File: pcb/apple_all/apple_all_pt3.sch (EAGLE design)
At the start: 47 parts, among them IC1 STM32F072C8T6, SW1 324_SW, SW2 324_SW, SW3 324_SW

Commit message: updated apple_all protocol card
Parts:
- removed U$1: PINHD1X4, adafruit_changed:PINHD1X4
- added JP8: (no value), pinhead:PINHD-1X2
- added R19: 2K, SparkFun-Passives:RESISTOR0805-RES
- R10, R16, R6, R8: value 50 -> 200
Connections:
- removed net N$30: IC1PORTB_L.PB1, JP5.1, R16.1
- new net N$11: IC1PORTB_L.PB1, U$10.4
- net GND: now also JP5.1, R16.1; no longer U$1.1
- net N$3: now also R19.2; no longer U$1.4
- net N$41: no longer U$10.4
- net N$43: no longer U$1.3
- net N$46: now also JP8.1, JP8.2, R19.1; no longer U$1.2

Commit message: added resistors on lisa pins
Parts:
- removed J4: (no value), SparkFun-Connectors:USB_C16PIN
- removed U$10: PINHD1X4, adafruit_changed:PINHD1X4
- added J1: (no value), SparkFun-Connectors:DB9FEMALE
- added R20: 5.1K, SparkFun-Passives:RESISTOR0805-RES
- added R21: 2K, SparkFun-Passives:RESISTOR0805-RES
- added U$1: M2.5HOLE, f1c100s:M2.5HOLE
- J2: device SparkFun-Connectors:DB9FEMALE -> SparkFun-Connectors:USB_C16PIN
- JP1: device adafruit_changed:PINHD-2X20-BIG -> pinhead:PINHD-1X5
- JP2: device pinhead:PINHD-2X3 -> pinhead:PINHD-1X2
- JP3: device pinhead:PINHD-2X4 -> pinhead:PINHD-2X2
- JP4: value AUDIO-JACK4-.25-HORIZ-TRS -> (none); device SparkFun-Connectors:AUDIO-JACK4-.25-HORIZ-TRS -> adafruit_changed:PINHD-2X20-BIG
- JP5: device pinhead:PINHD-2X2 -> pinhead:PINHD-2X3
- JP6: value (none) -> AUDIO-JACK4-.25-HORIZ-TRS; device pinhead:PINHD-1X5 -> SparkFun-Connectors:AUDIO-JACK4-.25-HORIZ-TRS
- JP8: device pinhead:PINHD-1X2 -> pinhead:PINHD-2X4
- R11: value 5.1K -> 200
- R12, R19: value 2K -> 5.1K
- R13, R17: value 5.1K -> 100
- R15: value 2K -> 100
- R16: value 200 -> 5.1K
- R18: value 100 -> 2K
- R6: value 200 -> 2K
- R7: value 2K -> 200
- R9: value 5.1K -> 2K
- U$3: value M2.5HOLE -> PINHD1X4; device f1c100s:M2.5HOLE -> adafruit_changed:PINHD1X4
- U$4: value ADB -> M2.5HOLE; device adb:ADB -> f1c100s:M2.5HOLE
- U$6: value M2.5HOLE -> ADB; device f1c100s:M2.5HOLE -> adb:ADB
- U$8: value PINHD1X4 -> RJ9PTH; device adafruit_changed:PINHD1X4 -> SparkFun-Retired:RJ9PTH
- U$9: value RJ9PTH -> PINHD1X4; device SparkFun-Retired:RJ9PTH -> adafruit_changed:PINHD1X4
- renumbered C7 to C1, C8 to C2, C9 to C3
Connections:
- new net N$30: JP6.RING, R15.1, R16.2
- new net N$32: JP6.TIP, R16.1, R17.1
- net +3V3: now also JP4.1, JP4.17, JP8.5, R12.2, SW3.2, SW3.3; no longer JP1.1, JP1.17, JP3.5, R9.2, SW2.2, SW2.3
- net +5V: now also J2.VBUS, JP4.2, JP4.4; no longer J4.VBUS, JP1.2, JP1.4
- net +7V: now also J1.4; no longer J2.4
- net GND: now also J1.3, J1.5, J1.SHIELD, J2.GND, J2.SHLD, JP3.1, JP4.14, JP4.20, JP4.25, JP4.30, JP4.34, JP4.39, JP4.6, JP4.9, JP5.2, JP8.6, R14.1, R19.2, R20.2, R9.1, SW2.1, SW2.4, U$3.1, U$6.GND, U$6.SHIELD; no longer J2.3, J2.5, J2.SHIELD, J4.GND, J4.SHLD, JP1.14, JP1.20, JP1.25, JP1.30, JP1.34, JP1.39, JP1.6, JP1.9, JP2.1, JP2.2, JP3.6, R14.2, R16.1, R18.2, R7.1, SW3.1, SW3.4, U$4.GND, U$4.SHIELD, U$8.1
- net N$1: now also J2.CC1, R19.1; no longer J4.CC1, R13.1
- net N$10: now also U$8.3; no longer U$9.3
- net N$11: now also U$9.4; no longer U$10.4
- net N$12: now also JP8.7; no longer JP3.7
- net N$13: now also JP4.22, R12.1, SW2.2, SW2.3; no longer JP1.22, R9.1, SW1.2, SW1.3
- net N$14: now also JP8.8; no longer JP3.8
- net N$15: now also JP8.3; no longer JP3.3
- net N$16: now also JP8.4; no longer JP3.4
- net N$17: now also JP3.2, R7.1; no longer JP5.2, R6.1
- net N$18: now also JP4.32, R14.2, SW3.1, SW3.4; no longer JP1.32, R11.2, SW2.1, SW2.4
- net N$19: now also JP3.4; no longer JP5.4
- net N$2: now also R18.2; no longer R12.2
- net N$20: now also U$8.2; no longer U$9.2
- net N$21: now also R11.2, U$8.1; no longer R16.2, U$9.1
- net N$22: now also JP4.5; no longer JP1.5
- net N$23: now also JP4.3; no longer JP1.3
- net N$24: now also JP6.EARTH, R13.1; no longer JP4.EARTH, R18.1
- net N$25: now also JP3.3; no longer JP5.3
- net N$26: now also J1.1, JP1.3; no longer J2.1, JP6.3
- net N$27: now also JP8.1, R21.1; no longer JP3.1, R15.1
- net N$28: now also R21.2; no longer R15.2
- net N$29: now also R9.2; no longer R7.2
- net N$3: now also R6.2, U$3.4, U$6.5V; no longer R19.2, U$4.5V, U$8.4
- net N$31: now also JP5.5, JP5.6, R17.2; no longer JP2.5, JP2.6, JP4.TIP, R17.1
- net N$34: now also J1.6, JP1.2; no longer J2.6, JP6.2
- net N$35: now also J1.7, JP1.5; no longer J2.7, JP6.5
- net N$36: now also J1.2, JP1.1; no longer J2.2, JP6.1
- net N$37: now also JP4.36; no longer JP1.36
- net N$38: now also U$9.1; no longer U$10.1
- net N$39: now also U$9.2; no longer U$10.2
- net N$4: now also J1.8, JP1.4; no longer J2.8, JP6.4
- net N$40: now also U$9.3; no longer U$10.3
- net N$41: now also JP5.3, JP5.4, R15.2; no longer JP2.3, JP2.4, JP4.RING, R17.2
- net N$43: now also U$3.3, U$6.ADB_DATA; no longer U$4.ADB_DATA, U$8.3
- net N$46: now also JP2.1, JP2.2, R6.1, SW1.2, SW1.3, U$3.2, U$6.PSW; no longer JP8.1, JP8.2, R19.1, SW3.2, SW3.3, U$4.PSW, U$8.2
- net N$5: now also R7.2, U$8.4; no longer R6.2, U$9.4
- net N$6: now also JP8.2, R18.1; no longer JP3.2, R12.1
- net N$7: now also J2.CC2, R20.1; no longer J4.CC2, R14.1
- net N$8: now also J2.D+; no longer J4.D+
- net N$9: now also J2.D-; no longer J4.D-
- net SPI_CS: now also JP4.24; no longer JP1.24
- net SPI_MISO: now also JP4.21; no longer JP1.21
- net SPI_MOSI: now also JP4.19; no longer JP1.19
- net SPI_SCK: now also JP4.23; no longer JP1.23
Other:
- moved on the sheet: R11, R12, R13, R14, R15, R16, R17, R18, R19, R6, R7, R9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

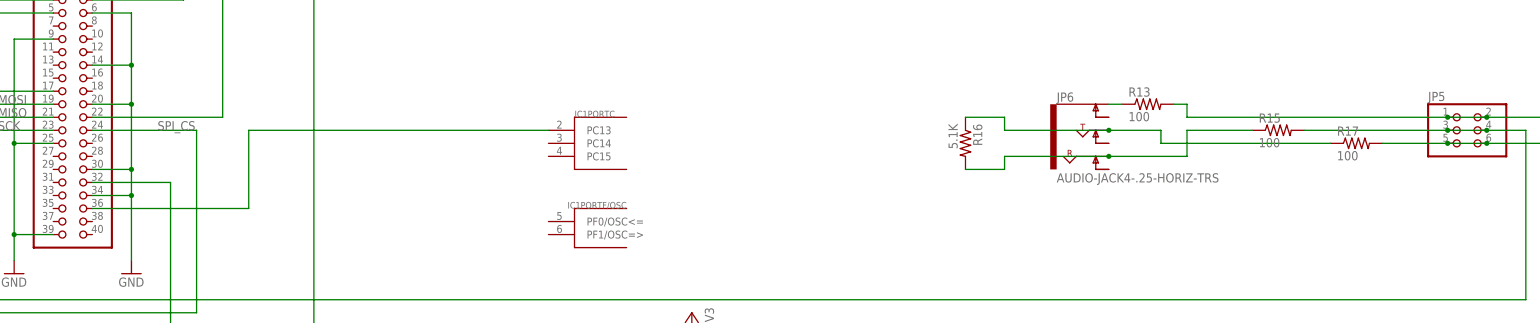
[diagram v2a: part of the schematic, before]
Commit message: added busy pin and adjusted resistors
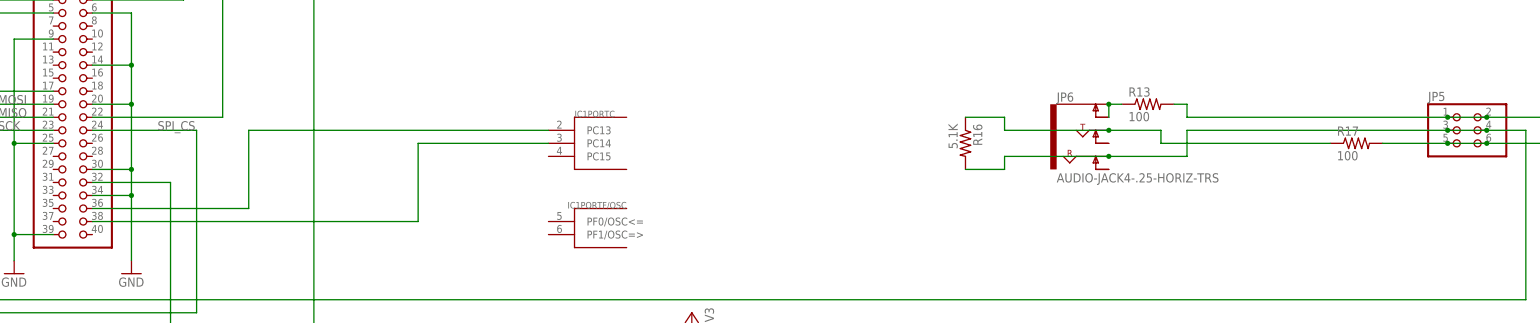
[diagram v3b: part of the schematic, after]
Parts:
- removed R15: 100, SparkFun-Passives:RESISTOR0805-RES
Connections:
- removed net N$41: IC1PORTA_L.PA3, JP5.3, JP5.4, R15.2
- new net N$33: IC1PORTC.PC14, JP4.38
- net N$24: now also JP6.EARTH-NORM
- net N$30: now also IC1PORTA_L.PA3, JP5.3, JP5.4; no longer R15.1
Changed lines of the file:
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@@
 <part name="JP2" library="pinhead" library_urn="urn:adsk.eagle:library:325" deviceset="PINHD-1X2" device="" package3d_urn="urn:adsk.eagle:package:22435/2"/>
 <part name="R6" library="SparkFun-Passives" deviceset="RESISTOR" device="0805-RES" value="2K"/>
-<part name="R15" library="SparkFun-Passives" deviceset="RESISTOR" device="0805-RES" value="100"/>
 <part name="R17" library="SparkFun-Passives" deviceset="RESISTOR" device="0805-RES" value="100"/>
 </parts>
@@
 <attribute name="VALUE" x="-31.242" y="128.27" size="1.778" layer="96" rot="MR90"/>
 </instance>
-<instance part="R15" gate="G$1" x="327.66" y="15.24" smashed="yes">
-<attribute name="NAME" x="323.85" y="16.7386" size="1.778" layer="95"/>
-<attribute name="VALUE" x="323.85" y="11.938" size="1.778" layer="96"/>
-</instance>
 <instance part="R17" gate="G$1" x="342.9" y="12.7" smashed="yes">
 <attribute name="NAME" x="339.09" y="14.1986" size="1.778" layer="95"/>
@@
 <pinref part="U$9" gate="1" pin="3"/>
 <wire x1="43.18" y1="22.86" x2="17.78" y2="22.86" width="0.1524" layer="91"/>
-</segment>
-</net>
-<net name="N$41" class="0">
-<segment>
-<pinref part="IC1" gate="PORTA_L" pin="PA3"/>
-<wire x1="43.18" y1="20.32" x2="20.32" y2="20.32" width="0.1524" layer="91"/>
-<wire x1="20.32" y1="-17.78" x2="375.92" y2="-17.78" width="0.1524" layer="91"/>
-<wire x1="375.92" y1="-17.78" x2="375.92" y2="15.24" width="0.1524" layer="91"/>
-<pinref part="JP5" gate="A" pin="4"/>
-<pinref part="JP5" gate="A" pin="3"/>
-<wire x1="360.68" y1="15.24" x2="368.3" y2="15.24" width="0.1524" layer="91"/>
-<junction x="360.68" y="15.24"/>
-<wire x1="375.92" y1="15.24" x2="368.3" y2="15.24" width="0.1524" layer="91"/>
-<junction x="368.3" y="15.24"/>
-<wire x1="20.32" y1="20.32" x2="20.32" y2="-17.78" width="0.1524" layer="91"/>
-<wire x1="332.74" y1="15.24" x2="360.68" y2="15.24" width="0.1524" layer="91"/>
-<pinref part="R15" gate="G$1" pin="2"/>
 </segment>
 </net>
@@
 <pinref part="R13" gate="G$1" pin="1"/>
 <wire x1="294.64" y1="20.32" x2="297.18" y2="20.32" width="0.1524" layer="91"/>
+<pinref part="JP6" gate="G$1" pin="EARTH-NORM"/>
+<wire x1="294.64" y1="17.78" x2="294.64" y2="20.32" width="0.1524" layer="91"/>
+<junction x="294.64" y="20.32"/>
 </segment>
 </net>
@@
 <segment>
 <pinref part="R16" gate="G$1" pin="2"/>
-<wire x1="309.88" y1="15.24" x2="322.58" y2="15.24" width="0.1524" layer="91"/>
 <wire x1="309.88" y1="10.16" x2="309.88" y2="15.24" width="0.1524" layer="91"/>
 <pinref part="JP6" gate="G$1" pin="RING"/>
@@
 <wire x1="274.32" y1="10.16" x2="274.32" y2="7.62" width="0.1524" layer="91"/>
 <wire x1="274.32" y1="7.62" x2="266.7" y2="7.62" width="0.1524" layer="91"/>
-<pinref part="R15" gate="G$1" pin="1"/>
+<pinref part="IC1" gate="PORTA_L" pin="PA3"/>
+<wire x1="43.18" y1="20.32" x2="20.32" y2="20.32" width="0.1524" layer="91"/>
+<wire x1="20.32" y1="-17.78" x2="375.92" y2="-17.78" width="0.1524" layer="91"/>
+<wire x1="375.92" y1="-17.78" x2="375.92" y2="15.24" width="0.1524" layer="91"/>
+<pinref part="JP5" gate="A" pin="4"/>
+<pinref part="JP5" gate="A" pin="3"/>
+<wire x1="360.68" y1="15.24" x2="368.3" y2="15.24" width="0.1524" layer="91"/>
+<junction x="360.68" y="15.24"/>
+<wire x1="375.92" y1="15.24" x2="368.3" y2="15.24" width="0.1524" layer="91"/>
+<junction x="368.3" y="15.24"/>
+<wire x1="20.32" y1="20.32" x2="20.32" y2="-17.78" width="0.1524" layer="91"/>
+<wire x1="309.88" y1="15.24" x2="360.68" y2="15.24" width="0.1524" layer="91"/>
 </segment>
 </net>
@@
 </segment>
 </net>
+<net name="N$33" class="0">
+<segment>
+<pinref part="IC1" gate="PORTC" pin="PC14"/>
+<wire x1="185.42" y1="12.7" x2="160.02" y2="12.7" width="0.1524" layer="91"/>
+<wire x1="160.02" y1="12.7" x2="160.02" y2="-2.54" width="0.1524" layer="91"/>
+<pinref part="JP4" gate="A" pin="38"/>
+<wire x1="160.02" y1="-2.54" x2="96.52" y2="-2.54" width="0.1524" layer="91"/>
+</segment>
+</net>

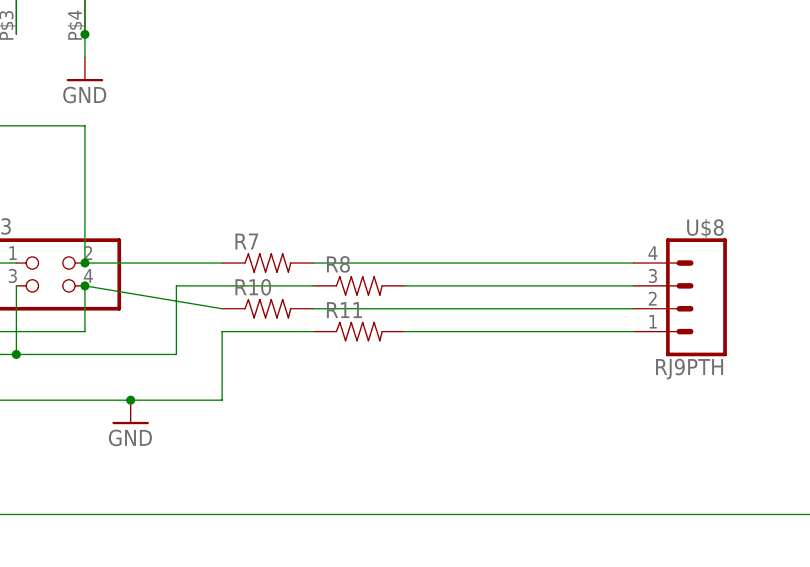
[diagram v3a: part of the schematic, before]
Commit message: m0110 keyboard working, added busy signal and protocol switching
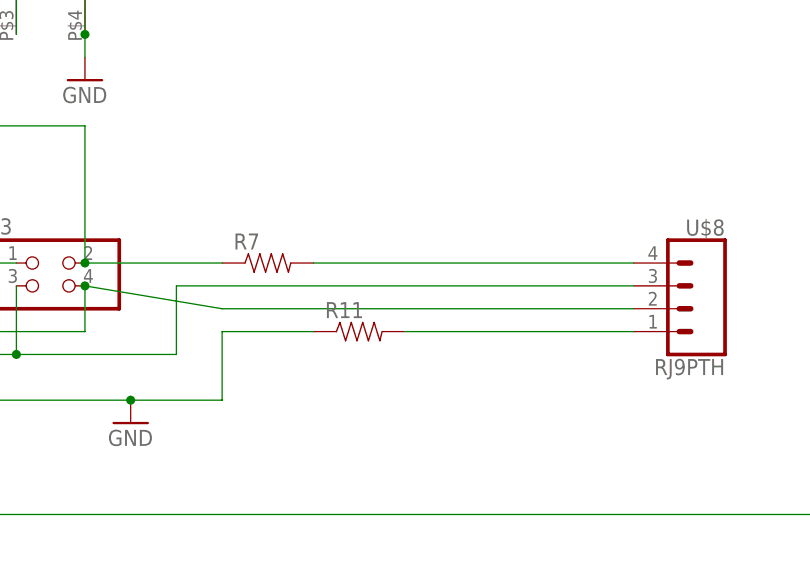
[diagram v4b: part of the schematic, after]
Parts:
- removed R10, R8: 200, SparkFun-Passives:RESISTOR0805-RES
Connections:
- removed net N$10: R8.2, U$8.3
- removed net N$20: R10.2, U$8.2
- net N$19: now also U$8.2; no longer R10.1
- net N$25: now also U$8.3; no longer R8.1
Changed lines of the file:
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@@
 <part name="JP1" library="pinhead" library_urn="urn:adsk.eagle:library:325" deviceset="PINHD-1X5" device="" package3d_urn="urn:adsk.eagle:package:22469/2"/>
 <part name="R7" library="SparkFun-Passives" deviceset="RESISTOR" device="0805-RES" value="200"/>
-<part name="R8" library="SparkFun-Passives" deviceset="RESISTOR" device="0805-RES" value="200"/>
-<part name="R10" library="SparkFun-Passives" deviceset="RESISTOR" device="0805-RES" value="200"/>
 <part name="R11" library="SparkFun-Passives" deviceset="RESISTOR" device="0805-RES" value="200"/>
 <part name="JP3" library="pinhead" library_urn="urn:adsk.eagle:library:325" deviceset="PINHD-2X2" device="" package3d_urn="urn:adsk.eagle:package:22455/2"/>
@@
 <attribute name="NAME" x="176.53" y="75.1586" size="1.778" layer="95"/>
 </instance>
-<instance part="R8" gate="G$1" x="190.5" y="71.12" smashed="yes">
-<attribute name="NAME" x="186.69" y="72.6186" size="1.778" layer="95"/>
-</instance>
-<instance part="R10" gate="G$1" x="180.34" y="68.58" smashed="yes">
-<attribute name="NAME" x="176.53" y="70.0786" size="1.778" layer="95"/>
-</instance>
 <instance part="R11" gate="G$1" x="190.5" y="66.04" smashed="yes">
 <attribute name="NAME" x="186.69" y="67.5386" size="1.778" layer="95"/>
@@
 </segment>
 </net>
-<net name="N$10" class="0">
-<segment>
-<pinref part="U$8" gate="G$1" pin="3"/>
-<wire x1="220.98" y1="71.12" x2="195.58" y2="71.12" width="0.1524" layer="91"/>
-<pinref part="R8" gate="G$1" pin="2"/>
-</segment>
-</net>
-<net name="N$20" class="0">
-<segment>
-<pinref part="U$8" gate="G$1" pin="2"/>
-<pinref part="R10" gate="G$1" pin="2"/>
-<wire x1="220.98" y1="68.58" x2="185.42" y2="68.58" width="0.1524" layer="91"/>
-</segment>
-</net>
 <net name="N$21" class="0">
 <segment>
@@
 <wire x1="96.52" y1="86.36" x2="96.52" y2="177.8" width="0.1524" layer="91"/>
 <wire x1="96.52" y1="177.8" x2="53.34" y2="177.8" width="0.1524" layer="91"/>
-<pinref part="R10" gate="G$1" pin="1"/>
 <wire x1="175.26" y1="68.58" x2="160.02" y2="71.12" width="0.1524" layer="91"/>
 <junction x="160.02" y="71.12"/>
+<pinref part="U$8" gate="G$1" pin="2"/>
+<wire x1="220.98" y1="68.58" x2="175.26" y2="68.58" width="0.1524" layer="91"/>
 </segment>
 </net>
 <net name="N$25" class="0">
 <segment>
-<pinref part="R8" gate="G$1" pin="1"/>
-<wire x1="185.42" y1="71.12" x2="170.18" y2="71.12" width="0.1524" layer="91"/>
+<wire x1="220.98" y1="71.12" x2="170.18" y2="71.12" width="0.1524" layer="91"/>
 <wire x1="170.18" y1="71.12" x2="170.18" y2="63.5" width="0.1524" layer="91"/>
 <pinref part="JP3" gate="A" pin="3"/>
@@
 <wire x1="152.4" y1="63.5" x2="134.62" y2="63.5" width="0.1524" layer="91"/>
 <junction x="152.4" y="63.5"/>
-</segment>
-</net>
+<pinref part="U$8" gate="G$1" pin="3"/>
+</segment>
+</net>
